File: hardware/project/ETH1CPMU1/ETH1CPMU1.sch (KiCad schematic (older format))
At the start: 0 parts

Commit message: Schematic design
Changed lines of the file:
@@
 $Descr A4 11693 8268
 encoding utf-8
-Sheet 1 12
+Sheet 1 14
 Title ""
 Date ""
@@
 $EndDescr
 $Sheet
-S 7900 3050 1750 1350
+S 10200 650  900  5700
 U 5DCED2F4
 F0 "Connector" 50
 F1 "Connector.sch" 50
-$EndSheet
-$Sheet
-S 2450 3800 2000 1650
+F2 "RX+" B L 10200 1750 50
+F3 "TX+" B L 10200 1550 50
+F4 "RX-" B L 10200 1850 50
+F5 "TX-" B L 10200 1650 50
+F6 "EXT_TRIG" B L 10200 2900 50
+F7 "A" B L 10200 750 50
+F8 "B" B L 10200 850 50
+F9 "C" B L 10200 950 50
+F10 "D" B L 10200 1050 50
+F11 "E" B L 10200 1150 50
+F12 "F" B L 10200 1250 50
+$EndSheet
+$Sheet
+S 7400 1450 1550 1750
 U 5DCED281
 F0 "MCU main" 50
 F1 "MCU_Main.sch" 50
-$EndSheet
-$Sheet
-S 1300 1650 1650 1200
+F2 "RMII_TXD1" B R 8950 1550 50
+F3 "RMII_TXD0" B R 8950 1650 50
+F4 "RMII_TXEN" B R 8950 1750 50
+F5 "RMII_RXD0" B R 8950 1850 50
+F6 "RMII_RXD1" B R 8950 1950 50
+F7 "RMII_CRS_DV" B R 8950 2050 50
+F8 "RMII_MDIO" B R 8950 2150 50
+F9 "RMII_MDC" B R 8950 2250 50
+F10 "REF_CLK" B R 8950 2350 50
+F11 "NRST" B R 8950 2450 50
+F12 "BASE_MCLK" O L 7400 1550 50
+F13 "BASE_MOSI" O L 7400 1650 50
+F14 "BASE_MISO" I L 7400 1750 50
+F15 "BASE_~MSS" O L 7400 1850 50
+F16 "TRIG_EN" O R 8950 2900 50
+F17 "TRIG_OUT" O R 8950 3000 50
+F18 "TRIG_IN" I R 8950 3100 50
+F19 "BASE_STATUS_IN" I L 7400 1950 50
+F20 "BASE_GPIO_OUT2" O L 7400 2050 50
+F21 "BASE_GPIO_OUT1" O L 7400 2150 50
+$EndSheet
+$Sheet
+S 9100 1450 950  1100
 U 5DD0AEA4
 F0 "Ethernet" 50
 F1 "Ethernet.sch" 50
-$EndSheet
-$Sheet
-S 5950 5150 1400 1050
+F2 "TX+" B R 10050 1550 50
+F3 "TX-" B R 10050 1650 50
+F4 "RX+" B R 10050 1750 50
+F5 "RX-" B R 10050 1850 50
+F6 "RMII_TXD1" B L 9100 1550 50
+F7 "RMII_TXD0" B L 9100 1650 50
+F8 "RMII_TXEN" B L 9100 1750 50
+F9 "RMII_RXD0" B L 9100 1850 50
+F10 "RMII_RXD1" B L 9100 1950 50
+F11 "RMII_CRS_DV" B L 9100 2050 50
+F12 "RMII_MDIO" B L 9100 2150 50
+F13 "RMII_MDC" B L 9100 2250 50
+F14 "NRST" B L 9100 2450 50
+F15 "REF_CLK" B L 9100 2350 50
+$EndSheet
+$Sheet
+S 6900 5300 3200 500
 U 5DD0B0B8
 F0 "Power base" 50
@@
 $EndSheet
 $Sheet
-S 2450 6450 1750 900
+S 7300 4450 2250 550
 U 5DD0DBE6
 F0 "Power float" 50
@@
 $EndSheet
 $Sheet
-S 6650 1500 1350 1150
+S 3750 1450 1650 6150
 U 5DF35BC8
 F0 "MCU second" 50
 F1 "MCU_Second.sch" 50
-$EndSheet
-$Sheet
-S 4750 2250 1500 1200
+F2 "PMU_STANDBY" O L 3750 7500 50
+F3 "PMU_~STB" O L 3750 7400 50
+F4 "PMU_CPCK" O L 3750 7300 50
+F5 "PMU_~MOE" O L 3750 7200 50
+F6 "PMU_~CS" O L 3750 7100 50
+F7 "PMU_AM0" O L 3750 7000 50
+F8 "PMU_AM1" O L 3750 6900 50
+F9 "PMU_AM2" O L 3750 6800 50
+F10 "PMU_MSEL" O L 3750 6700 50
+F11 "PMU_AC0" O L 3750 6600 50
+F12 "PMU_AC1" O L 3750 6500 50
+F13 "PMU_CPOH" I L 3750 6400 50
+F14 "PMU_CPOL" I L 3750 6300 50
+F15 "PMU_CLHDETECT" I L 3750 6200 50
+F16 "PMU_CLLDETECT" I L 3750 6100 50
+F17 "PMU_QM4" I L 3750 6000 50
+F18 "PMU_QM5" I L 3750 5900 50
+$EndSheet
+$Sheet
+S 2450 1450 1150 700
+U 5DF36C0B
+F0 "DC source" 50
+F1 "DC_Source.sch" 50
+F2 "DC_FOURCE" O L 2450 1550 50
+F3 "DC_DAC_~CLR" I R 3600 1550 50
+F4 "DC_DAC_~LDAC" I R 3600 1650 50
+F5 "DC_DAC_SDO" O R 3600 1750 50
+F6 "DC_DAC_~SYNC" I R 3600 1850 50
+F7 "DC_DAC_SCLK" I R 3600 1950 50
+F8 "DC_DAC_SDIN" I R 3600 2050 50
+$EndSheet
+$Sheet
+S 2450 2350 1150 600
+U 5DF36C25
+F0 "AC source" 50
+F1 "AC_Source.sch" 50
+$EndSheet
+$Sheet
+S 2450 3150 1150 700
+U 5DF36C38
+F0 "ADC" 50
+F1 "ADC.sch" 50
+$EndSheet
+$Sheet
+S 2450 4100 1150 750
+U 5DF36C70
+F0 "DAC" 50
+F1 "DAC.sch" 50
+$EndSheet
+Wire Wire Line
+	9100 2450 8950 2450
+Wire Wire Line
+	8950 2350 9100 2350
+Wire Wire Line
+	9100 2250 8950 2250
+Wire Wire Line
+	8950 2150 9100 2150
+Wire Wire Line
+	9100 2050 8950 2050
+Wire Wire Line
+	8950 1950 9100 1950
+Wire Wire Line
+	9100 1850 8950 1850
+Wire Wire Line
+	8950 1750 9100 1750
+Wire Wire Line
+	8950 1650 9100 1650
+Wire Wire Line
+	9100 1550 8950 1550
+$Sheet
+S 9100 2800 950  400
+U 5DD52C08
+F0 "Trigger" 50
+F1 "Trigger.sch" 50
+F2 "EXT_TRIG" B R 10050 2900 50
+F3 "TRIG_EN" I L 9100 2900 50
+F4 "TRIG_OUT" I L 9100 3000 50
+F5 "TRIG_IN" O L 9100 3100 50
+$EndSheet
+Wire Wire Line
+	9100 2900 8950 2900
+Wire Wire Line
+	8950 3000 9100 3000
+Wire Wire Line
+	9100 3100 8950 3100
+Wire Wire Line
+	10200 2900 10050 2900
+Wire Wire Line
+	10200 1850 10050 1850
+Wire Wire Line
+	10050 1750 10200 1750
+Wire Wire Line
+	10200 1650 10050 1650
+Wire Wire Line
+	10200 1550 10050 1550
+$Sheet
+S 5600 1450 1650 800
+U 5DD672F1
+F0 "Isolation" 50
+F1 "Isolation.sch" 50
+F2 "MAIN_GPIO_OUT1" I R 7250 2050 50
+F3 "MAIN_~MSS" I R 7250 1850 50
+F4 "MAIN_MISO" O R 7250 1750 50
+F5 "MAIN_MOSI" I R 7250 1650 50
+F6 "MAIN_MCLK" I R 7250 1550 50
+F7 "MAIN_STATUS_IN" O R 7250 1950 50
+F8 "MAIN_GPIO_OUT2" I R 7250 2150 50
+F9 "SECOND_~SSS" O L 5600 1850 50
+F10 "SECOND_MISO" I L 5600 1750 50
+F11 "SECOND_MOSI" O L 5600 1650 50
+F12 "SECOND_SCLK" O L 5600 1550 50
+F13 "SECOND_GPIO_OUT1" O L 5600 2050 50
+F14 "SECOND_STATUS_IN" I L 5600 1950 50
+F15 "SECOND_GPIO_OUT2" O L 5600 2150 50
+$EndSheet
+$Sheet
+S 900  600  1400 7000
 U 5DF36410
 F0 "PMU" 50
 F1 "PMU.sch" 50
-$EndSheet
-$Sheet
-S 5950 4150 1500 750
-U 5DF36C0B
-F0 "DC source" 50
-F1 "DC_Source.sch" 50
-$EndSheet
-$Sheet
-S 8250 5000 1500 950
-U 5DF36C25
-F0 "AC source" 50
-F1 "AC_Source.sch" 50
-$EndSheet
-$Sheet
-S 3850 800  1450 1050
-U 5DF36C38
-F0 "ADC" 50
-F1 "ADC.sch" 50
-$EndSheet
-$Sheet
-S 8950 1250 1550 1100
-U 5DF36C70
-F0 "DAC" 50
-F1 "DAC.sch" 50
-$EndSheet
+F2 "PMU_STANDBY" I R 2300 7500 50
+F3 "PMU_~STB" I R 2300 7400 50
+F4 "PMU_CPCK" I R 2300 7300 50
+F5 "PMU_~MOE" I R 2300 7200 50
+F6 "PMU_~CS" I R 2300 7100 50
+F7 "PMU_AM0" I R 2300 7000 50
+F8 "PMU_AM1" I R 2300 6900 50
+F9 "PMU_AM2" I R 2300 6800 50
+F10 "PMU_MSEL" I R 2300 6700 50
+F11 "PMU_AC0" I R 2300 6600 50
+F12 "PMU_AC1" I R 2300 6500 50
+F13 "PMU_CPOH" O R 2300 6400 50
+F14 "PMU_CPOL" O R 2300 6300 50
+F15 "PMU_CLHDETECT" O R 2300 6200 50
+F16 "PMU_CLLDETECT" O R 2300 6100 50
+F17 "PMU_QM4" O R 2300 6000 50
+F18 "PMU_QM5" O R 2300 5900 50
+$EndSheet
+Wire Wire Line
+	2300 7500 3750 7500
+Wire Wire Line
+	3750 7400 2300 7400
+Wire Wire Line
+	2300 7300 3750 7300
+Wire Wire Line
+	3750 7200 2300 7200
+Wire Wire Line
+	2300 7100 3750 7100
+Wire Wire Line
+	3750 7000 2300 7000
+Wire Wire Line
+	2300 6900 3750 6900
+Wire Wire Line
+	2300 6800 3750 6800
+Wire Wire Line
+	2300 6700 3750 6700
+Wire Wire Line
+	3750 6600 2300 6600
+Wire Wire Line
+	2300 6500 3750 6500
+Wire Wire Line
+	3750 6400 2300 6400
+Wire Wire Line
+	2300 6300 3750 6300
+Wire Wire Line
+	3750 6200 2300 6200
+Wire Wire Line
+	2300 6100 3750 6100
+Wire Wire Line
+	3750 6000 2300 6000
+Wire Wire Line
+	2300 5900 3750 5900
+Wire Wire Line
+	2450 1550 2300 1550
+Wire Wire Line
+	7400 1550 7250 1550
+Wire Wire Line
+	7250 1650 7400 1650
+Wire Wire Line
+	7400 1750 7250 1750
+Wire Wire Line
+	7250 1850 7400 1850
+Wire Wire Line
+	7400 1950 7250 1950
+Wire Wire Line
+	7250 2050 7400 2050
+Wire Wire Line
+	7400 2150 7250 2150
 $EndSCHEMATC

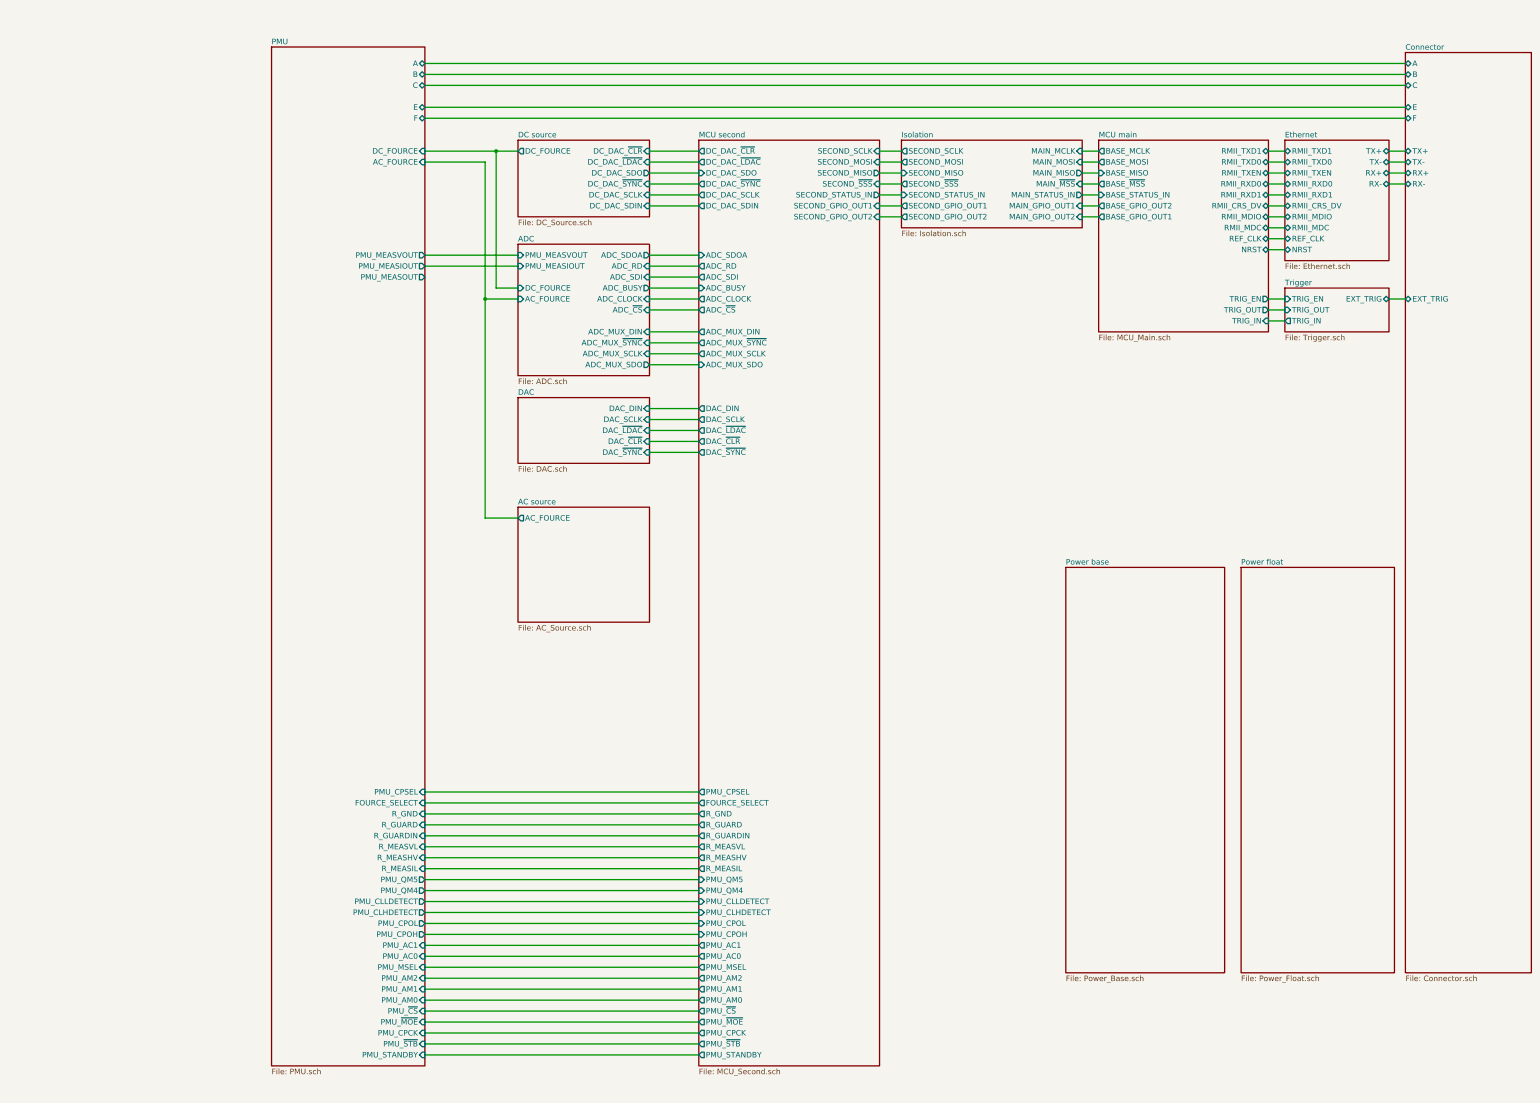
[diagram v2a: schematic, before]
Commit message: Function generator schematic design.
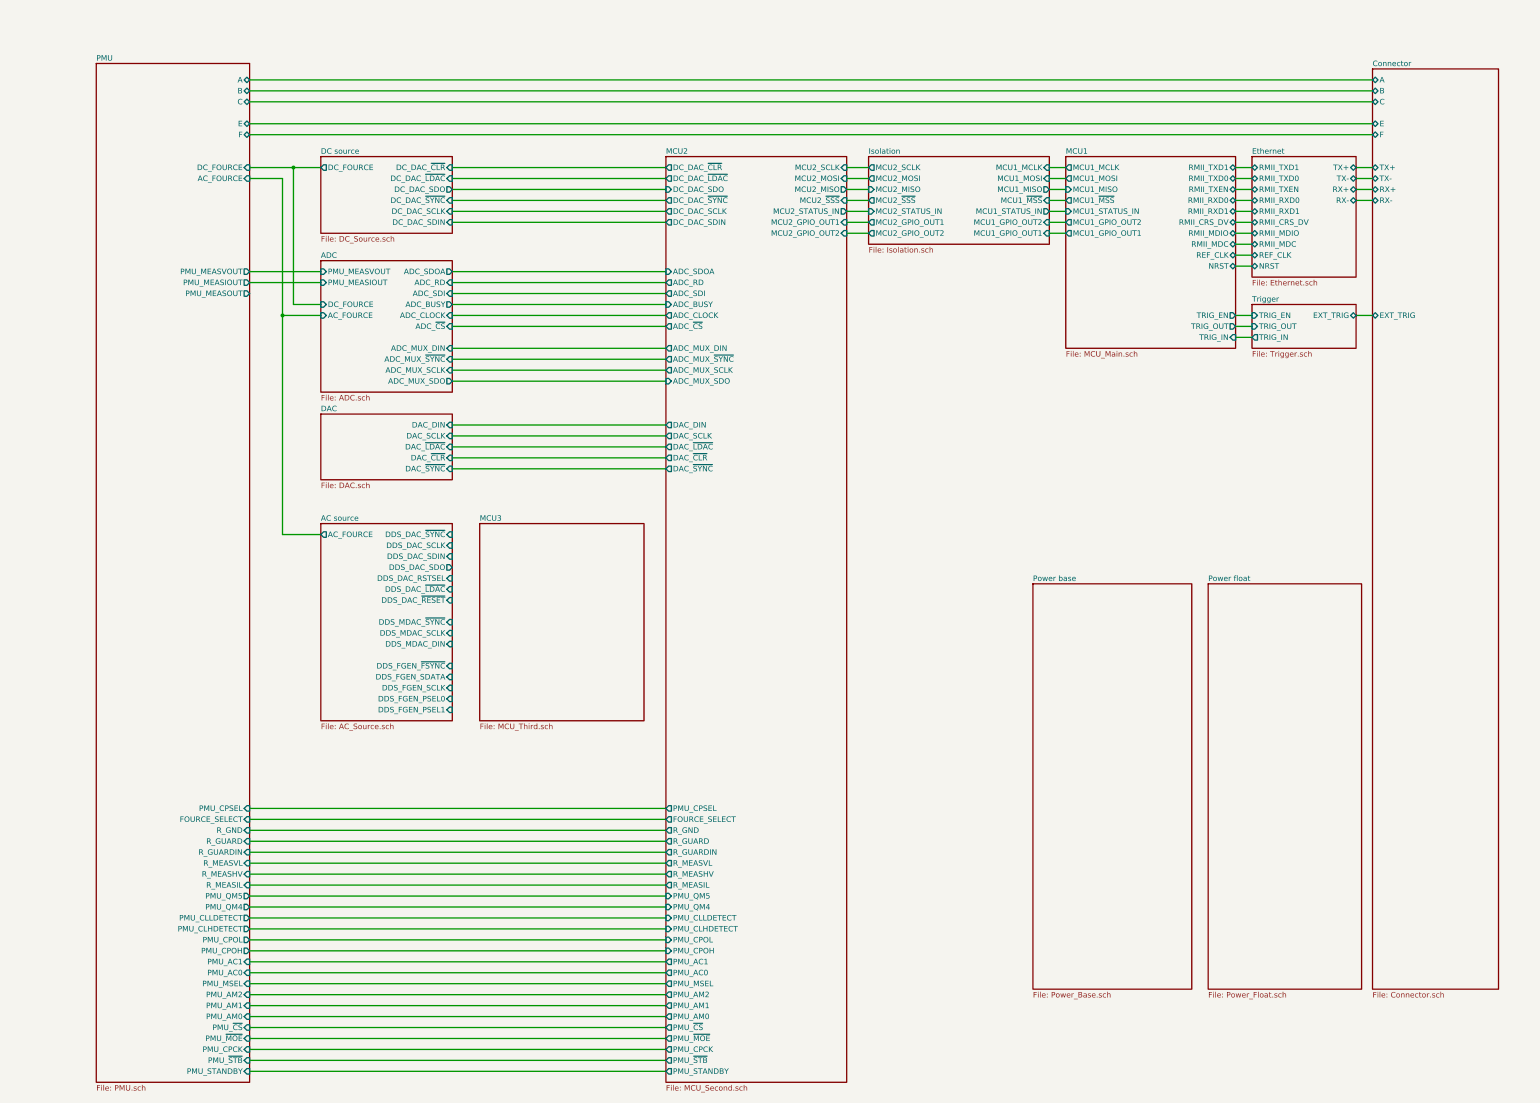
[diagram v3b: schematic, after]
